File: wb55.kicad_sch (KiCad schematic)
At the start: 30 parts, among them J2 Conn_02x05_Counter_Clockwise, U3 STM32WB55RGVx, Y1 nx2012_32768, Y2 nx2016_32m

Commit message: schematics: cleanup bom
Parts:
- C17: value 10uF 6.3v -> 4.7uF
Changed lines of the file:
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@@
 			)
 		)
-		(property "Value" "10uF 6.3v"
+		(property "Value" "4.7uF"
 			(at 204.978 28.194 0)
 			(effects

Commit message: 1.0.0 boards sent to production
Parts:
- AE2: LCSC (none) -> C2651048
- AE3: now left out of the parts list
- C10, C11, C12, C13, C14, C16, C18, C5, C6, C9: LCSC (none) -> C1525
- C15: LCSC (none) -> C15195
- C17: LCSC (none) -> C19666; pn (none) -> C19666
- C4: LCSC (none) -> C1546
- C7, C8: LCSC (none) -> C1547
- L1: LCSC (none) -> C19666; now not fitted
- L2: LCSC (none) -> C19666
- L3: now not fitted
- L4, R2: LCSC (none) -> C17168
- L5: LCSC (none) -> C77107
- R14: LCSC (none) -> C25767
- R4: LCSC (none) -> C25158
- U3: LCSC (none) -> C401505
- Y2: LCSC (none) -> C1986260
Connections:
- net ant_path: now reaches AE2.1 (OUT), L2.2, L3.2
- net ANT renamed pi_to_ant
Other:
- note added: "0.245 @ aisler 4layer HD boards 0.293 @ JLC 7678 boards (0.2 trace to copper)"
- note removed: "0.245 @ aisler 4layer HD boards"
- moved on the sheet: AE3

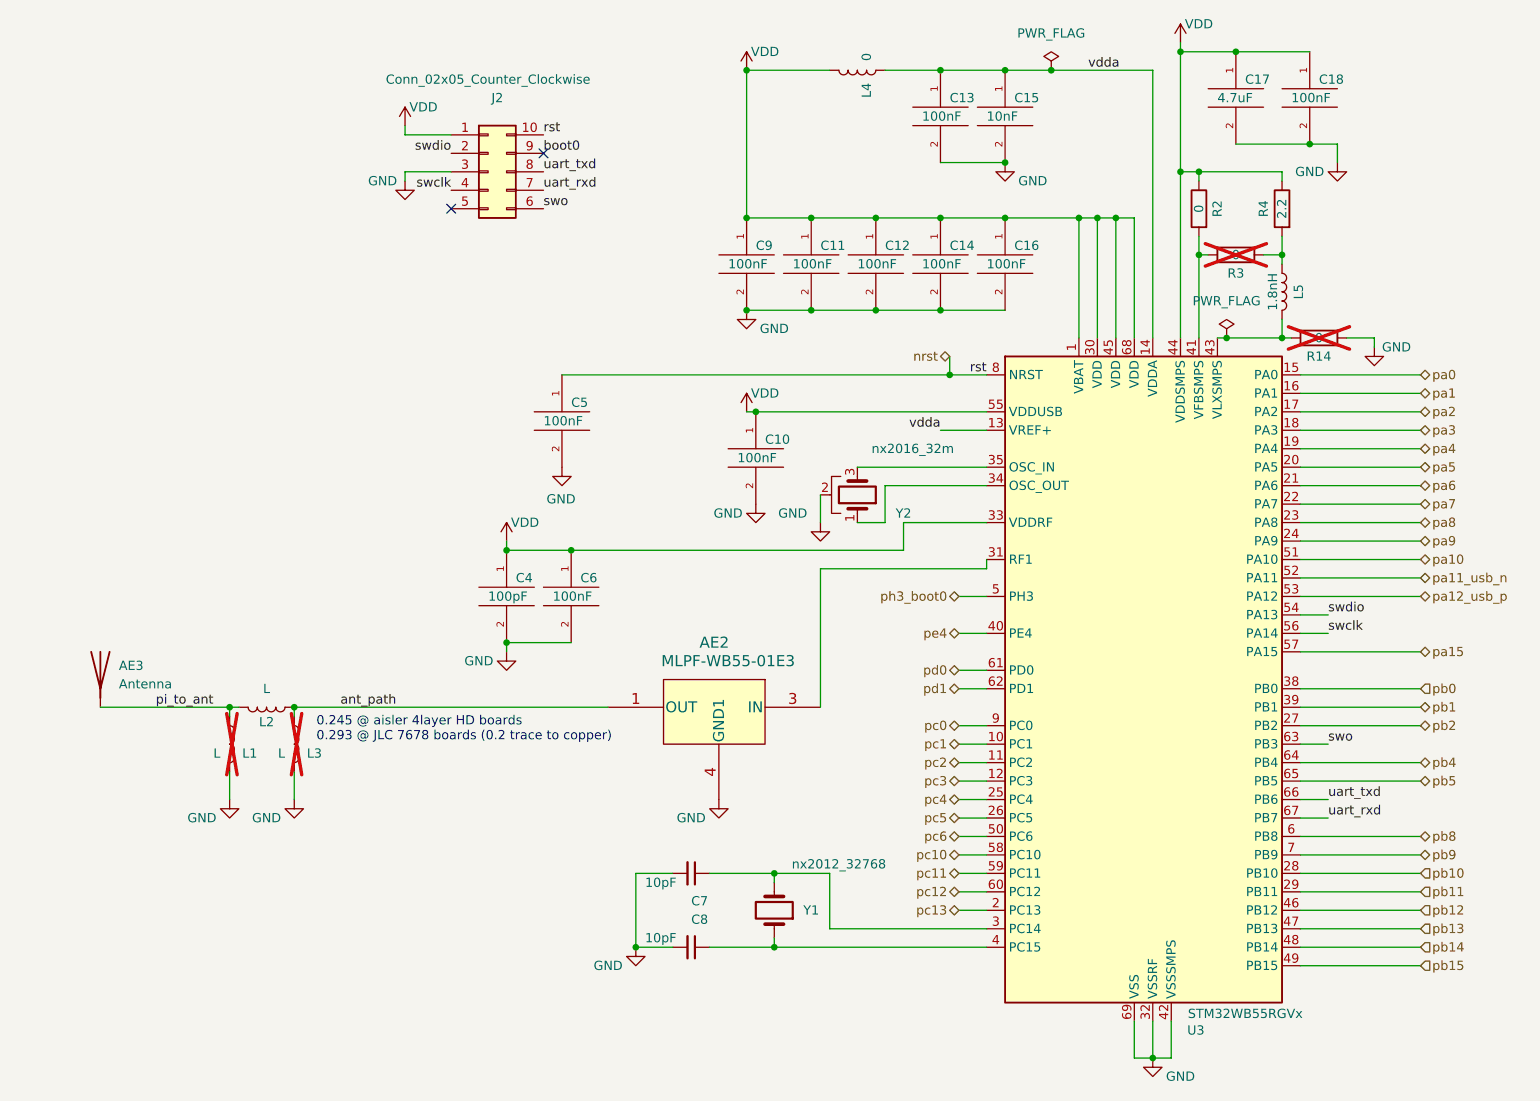
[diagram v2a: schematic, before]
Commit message: cleanups, exclude some drcs, fix antenna symbol to avoid ground disconnection, tweak ci
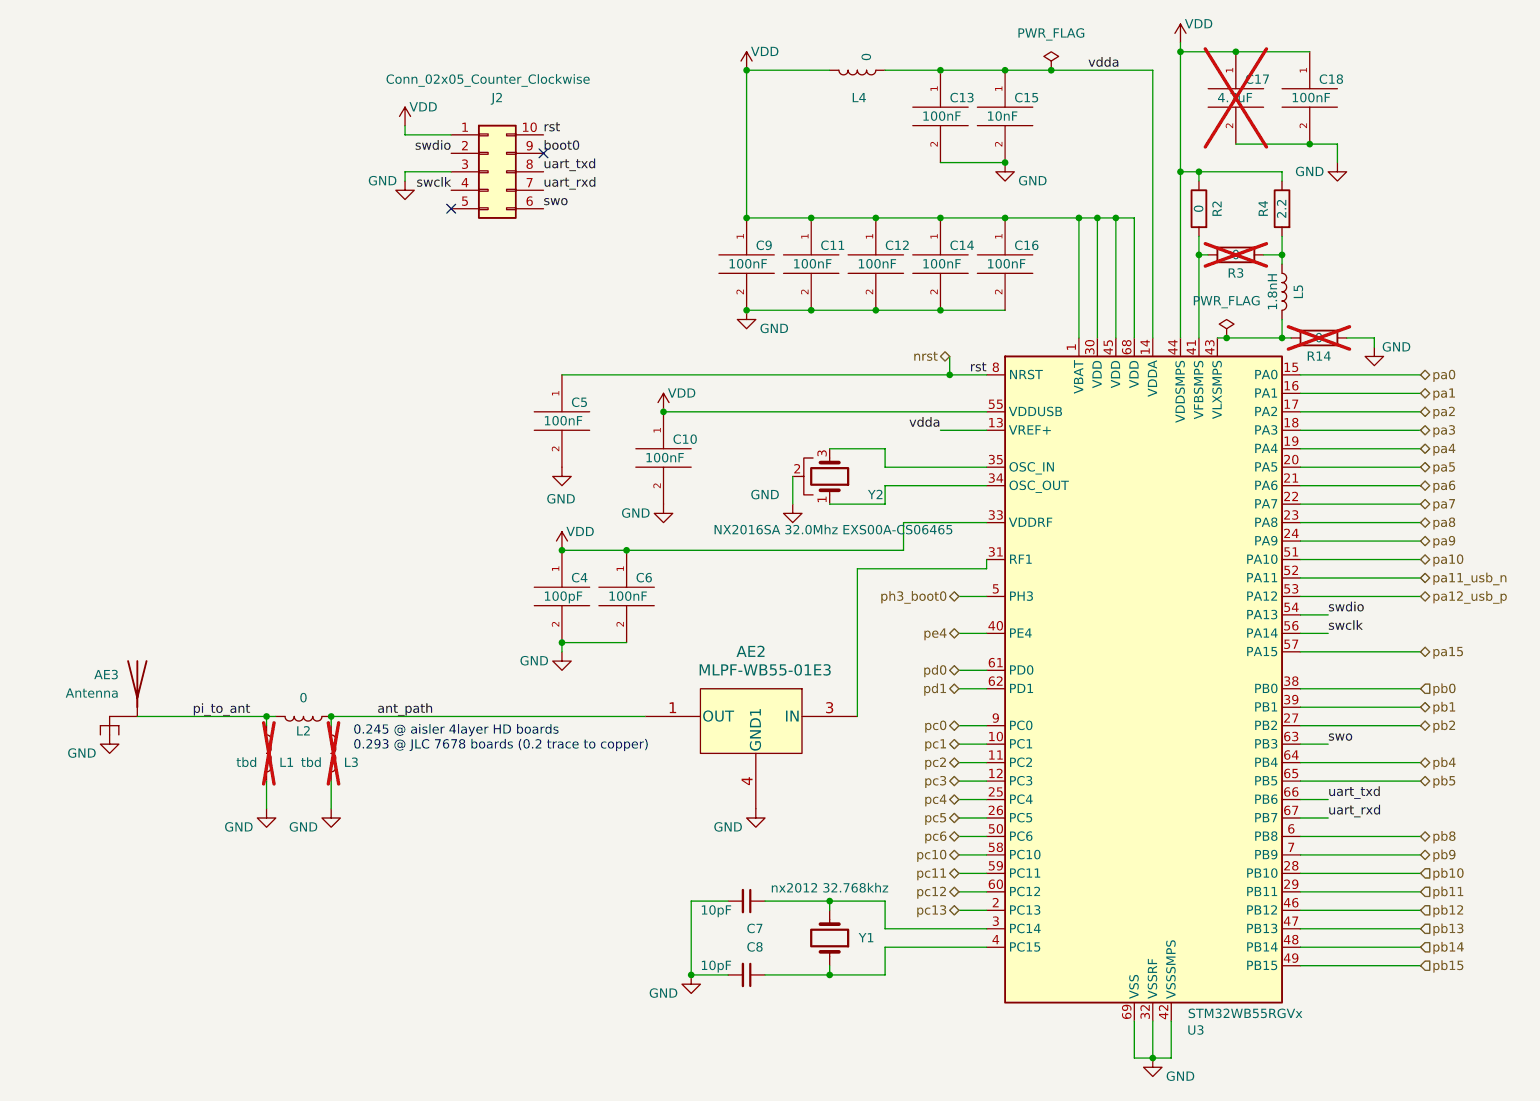
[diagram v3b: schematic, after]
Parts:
- C17: now not fitted
- L1, L3: value L -> tbd
- L2: value L -> 0
- Y1: value nx2012_32768 -> nx2012 32.768khz
- Y2: value nx2016_32m -> NX2016SA 32.0Mhz EXS00A-CS06465
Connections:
- net GND: now also AE3.2 (gnd)
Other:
- moved on the sheet: AE2, C10, C4, C6, C7, C8, L1, L2, L3, Y1, Y2
